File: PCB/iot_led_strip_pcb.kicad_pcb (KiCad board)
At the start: 2 copper layers, 50 x 50 mm, 61 parts, among them J1 I2C Expansion, J2 Conn_01x03_Socket, J3 GT-USB-7010ASV, J4 Barrel_Jack_Switch_Pin3Ring, J5 TC2050-IDC_Cortex-M, J6 Conn_01x03_Socket_Solderwire, J7 PWR_HEADER, J8 UART, Q1 BSS138, SW1 RESET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

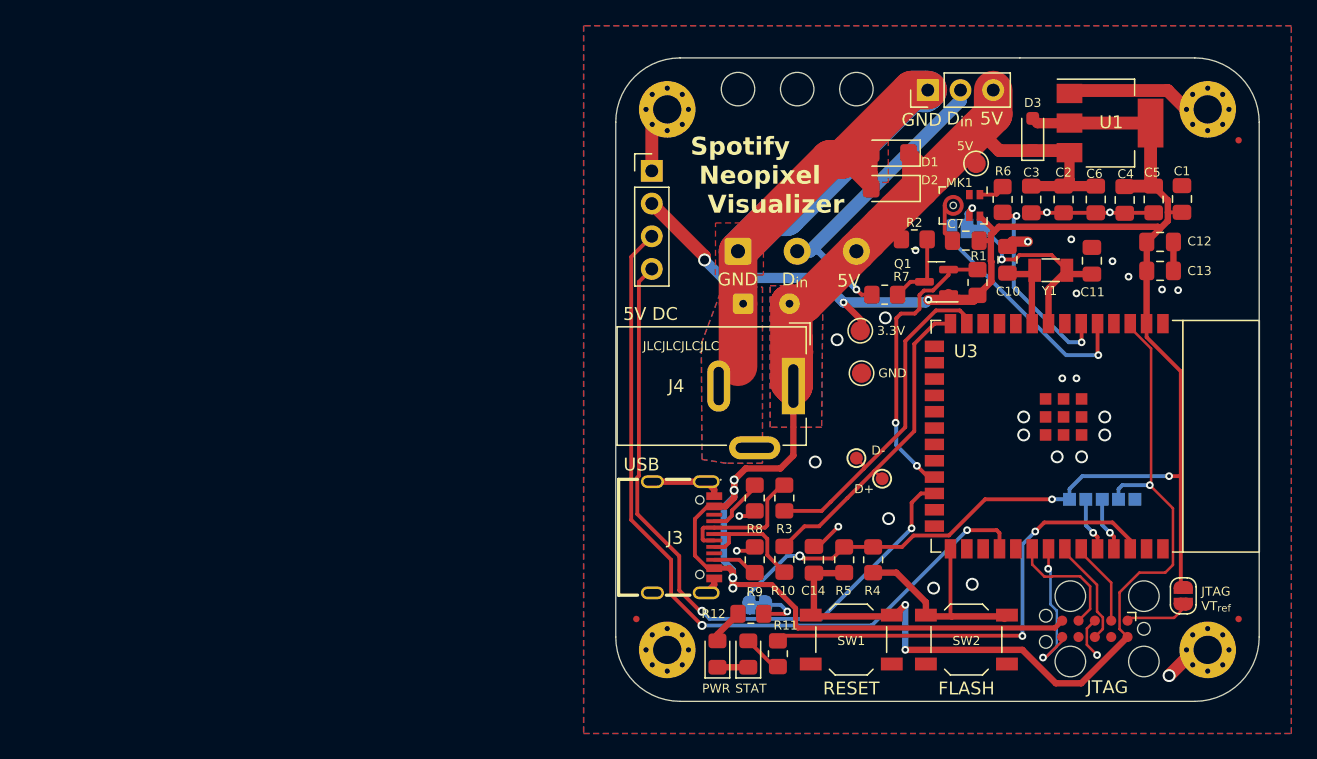
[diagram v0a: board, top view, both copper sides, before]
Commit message: Major schematic update for v2.3
This was my first real PCB project, and looking back with a couple
months of hindsight I made some mistakes. Some best practices for
driving WS2812B strips weren't followed in my original version, and
I've updated the schematic to reflect what I've learned and what
improvements needed to be made.

* Warning added to README about current version
* Schematic reorganized into tiles
* RTC clock removed
* OLED and I2C headers removed
* JTAG footprint updated
* Pin header output replaced with screw terminal
* Hole size for power injection header increased
* Added whole system fuse and PTC fuse to protect ESP32
* Added reverse polarity protection and re-added ability to disconnect
  USB Vbus from Vdd, so it's possible to program when the strip is
  connected to 12V without frying your computer

There are a couple other improvements that could still be made to the
schematic (removing the solderwire connector for example) but it remains to
be seen if I'm going to go back and re-design the PCB to incorporate
these changes or move onto newer projects.
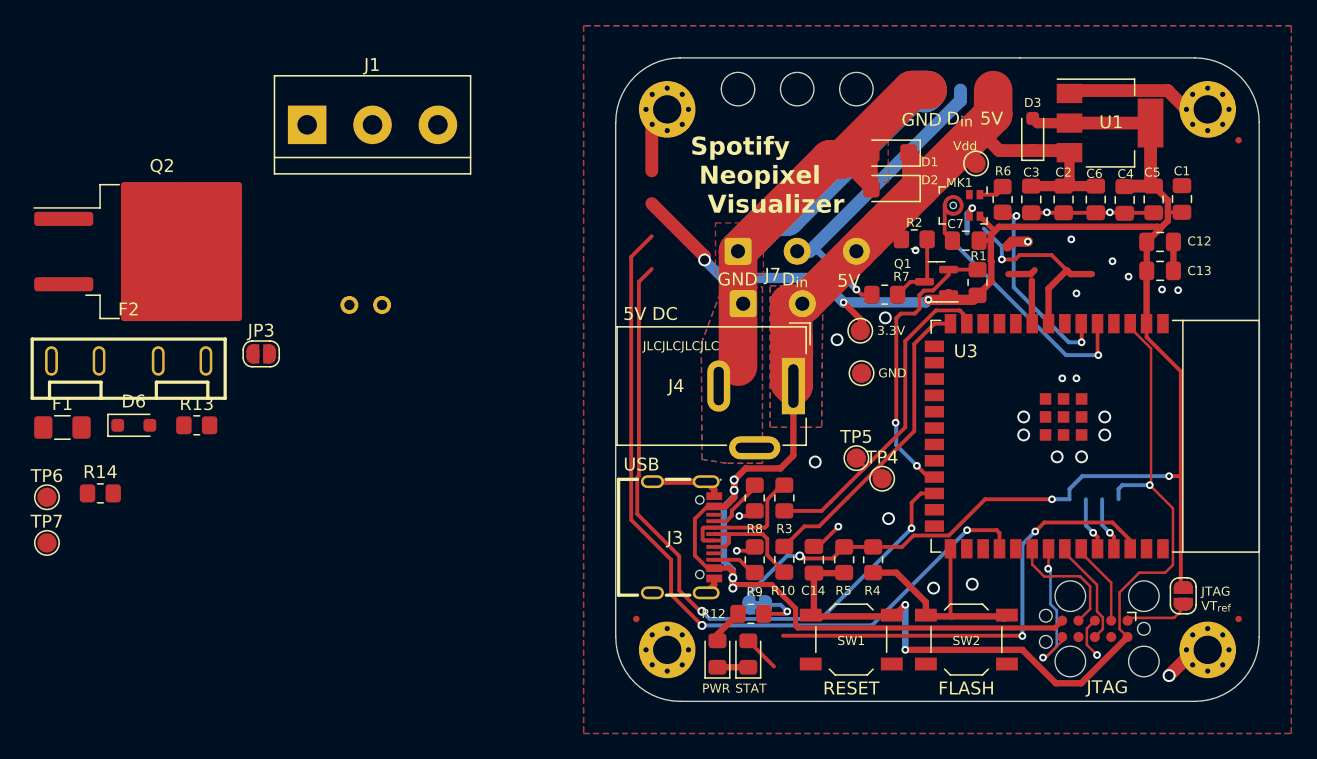
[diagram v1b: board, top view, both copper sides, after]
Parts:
- removed C10, C11: 22pF, Capacitor_SMD:C_0805_2012Metric_Pad1.18x1.45mm_HandSolder
- removed J2: Conn_01x03_Socket, Connector_PinHeader_2.54mm:PinHeader_1x03_P2.54mm_Vertical
- removed J8: UART, footprint:5 Pin Pad array
- removed R11: 100, Resistor_SMD:R_0805_2012Metric_Pad1.20x1.40mm_HandSolder
- removed Y1: Crystal 32kHz, Crystal:Crystal_SMD_3215-2Pin_3.2x1.5mm
- added D6: 1N5819WS, Diode_SMD:D_SOD-323_HandSoldering, F.Cu at (72.5, 98.5)
- added F1: 36V 1A Polyfuse, Fuse:Fuse_1206_3216Metric_Pad1.42x1.75mm_HandSolder, F.Cu at (67.0, 98.7)
- added F2: Fuse Holder, jmux-footprints:FUSE-TH_XF-505P, F.Cu at (72.2, 93.5)
- added JP3: USB-VCC, Jumper:SolderJumper-2_P1.3mm_Open_RoundedPad1.0x1.5mm, F.Cu at (82.5, 93.0)
- added Q2: IRF9Z34NS, Package_TO_SOT_SMD:TO-263-2, F.Cu at (74.8, 85.0)
- added R13: 10k, Resistor_SMD:R_0805_2012Metric_Pad1.20x1.40mm_HandSolder, F.Cu at (77.4, 98.5)
- added R14: 1k, Resistor_SMD:R_0805_2012Metric_Pad1.20x1.40mm_HandSolder, F.Cu at (70.0, 103.8)
- added TP6: TX, TestPoint:TestPoint_Pad_D1.5mm, F.Cu at (65.8, 104.1)
- added TP7: RX, TestPoint:TestPoint_Pad_D1.5mm, F.Cu at (65.8, 107.7)
- J1: value I2C Expansion -> Screw_Terminal_01x03; footprint Connector_PinHeader_2.54mm:PinHeader_1x04_P2.54mm_Vertical -> TerminalBlock:TerminalBlock_bornier-3_P5.08mm
- J5: value TC2050-IDC_Cortex-M -> TC2050-JTAG
- J7: footprint Connector_Wire:SolderWire-0.1sqmm_1x02_P3.6mm_D0.4mm_OD1mm -> Connector_Wire:SolderWire-0.5sqmm_1x02_P4.6mm_D0.9mm_OD2.1mm
- JP1: value MIC_CLK_SEL -> Jumper_2_Open; footprint Jumper:SolderJumper-3_P1.3mm_Bridged12_RoundedPad1.0x1.5mm -> TestPoint:TestPoint_2Pads_Pitch2.54mm_Drill0.8mm
- R12: value 100 -> 1k
- TP1: value 5V -> Vdd
- TP4, TP5: footprint TestPoint:TestPoint_Pad_D1.0mm -> TestPoint:TestPoint_Pad_D1.5mm
- moved JP1 45.8 mm to (91.8, 89.2)
- moved J1 27.0 mm to (86.0, 75.2)
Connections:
- net /~{RST} renamed ~{RST}
- C2 pad 1: +5V -> Net-(D6-K)
- C3 pad 1: +5V -> Net-(D6-K)
- C6 pad 1: +5V -> Net-(D6-K)
- D1 pad 1: +5V -> Net-(D1-A1)
- D2 pad 1: +5V -> Net-(D1-A1)
- D3 pad 1: +5V -> Net-(D3-K)
- J1 pad 2: +3.3V -> /D_{IN}
- J1 pad 3: /SCL -> VDD
- J3 pad A4B9: +5V -> VBUS
- J3 pad B4A9: +5V -> VBUS
- J4 pad 1: +5V -> VDD
- J5 pad 5: +5V -> Earth
- J6 pad 3: +5V -> VDD
- J7 pad 2: +5V -> Net-(D6-K)
- JP1 pad 1: /XP -> VBUS
- JP1 pad 2: Net-(JP1-C) -> VDD
- MK1 pad 4: Net-(JP1-C) -> /MIC_CLK
- R12 pad 1: Net-(D5-A) -> Net-(D4-A)
- R12 pad 2: Net-(JP2-A) -> Net-(U3-GPIO2/TOUCH2/ADC1_CH1)
- R2 pad 1: +5V -> VDD
- TP1 pad 1: +5V -> Net-(D6-K)
- U1 pad 3: +5V -> Net-(D3-K)
- U3 pad 24: /SDA -> unconnected-(U3-SPIIO4/GPIO33/FSPIHD-Pad24)
- U3 pad 30: /SCL -> unconnected-(U3-SPIDQS/GPIO37/FSPIQ-Pad30)
- U3 pad 36: /UART_TX -> Net-(U3-U0RXD/GPIO44/CLK_OUT2)
- U3 pad 37: /UART_RX -> Net-(U3-U0TXD/GPIO43/CLK_OUT1)
- U3 pad 8: /XP -> unconnected-(U3-GPIO15/U0RTS/ADC2_CH4/XTAL_32K_P-Pad8)
- U3 pad 9: /XN -> unconnected-(U3-GPIO16/U0CTS/ADC2_CH5/XTAL_32K_N-Pad9)
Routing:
- net (no net): track 0.00 -> 128.7 mm
- net +5V: track 126.5 -> 0.00 mm, vias 4 -> 0
- net unconnected-(U3-SPIDQS/GPIO37/FSPIQ-Pad30): track 0.00 -> 60.7 mm, vias 0 -> 2
- net /SCL: track 60.7 -> 0.00 mm, vias 2 -> 0
- net unconnected-(U3-SPIIO4/GPIO33/FSPIHD-Pad24): track 0.00 -> 52.7 mm, vias 0 -> 2
- net /SDA: track 52.7 -> 0.00 mm, vias 2 -> 0
- net unconnected-(U3-GPIO15/U0RTS/ADC2_CH4/XTAL_32K_P-Pad8): track 0.00 -> 15.5 mm, vias 0 -> 1
- net /XP: track 15.5 -> 0.00 mm, vias 1 -> 0
- net /XN: track 5.49 -> 0.00 mm
- net Net-(U3-U0TXD/GPIO43/CLK_OUT1): track 0.00 -> 4.23 mm, vias 0 -> 1
- net Net-(U3-U0RXD/GPIO44/CLK_OUT2): track 0.00 -> 4.23 mm, vias 0 -> 1
- net /UART_TX: track 4.23 -> 0.00 mm, vias 1 -> 0
- net /UART_RX: track 4.23 -> 0.00 mm, vias 1 -> 0
- net unconnected-(U3-GPIO16/U0CTS/ADC2_CH5/XTAL_32K_N-Pad9): track 0.00 -> 3.33 mm
- net Net-(JP1-C): track 2.81 -> 0.00 mm, vias 1 -> 0
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- added copper zone on B.Cu, net VDD
- added copper zone on F.Cu, net VDD
- removed copper zone on B.Cu, net +5V
- removed copper zone on F.Cu, net +5V
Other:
- board text added: "PCB3D_BR_iotleddriverhw"
- board text added: "PCB3D_TL_iotleddriverhw"
